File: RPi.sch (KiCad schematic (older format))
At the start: 8 parts, among them U3 LMS6002DR2, U4 ECP5, X3 RaspberryPiConnector

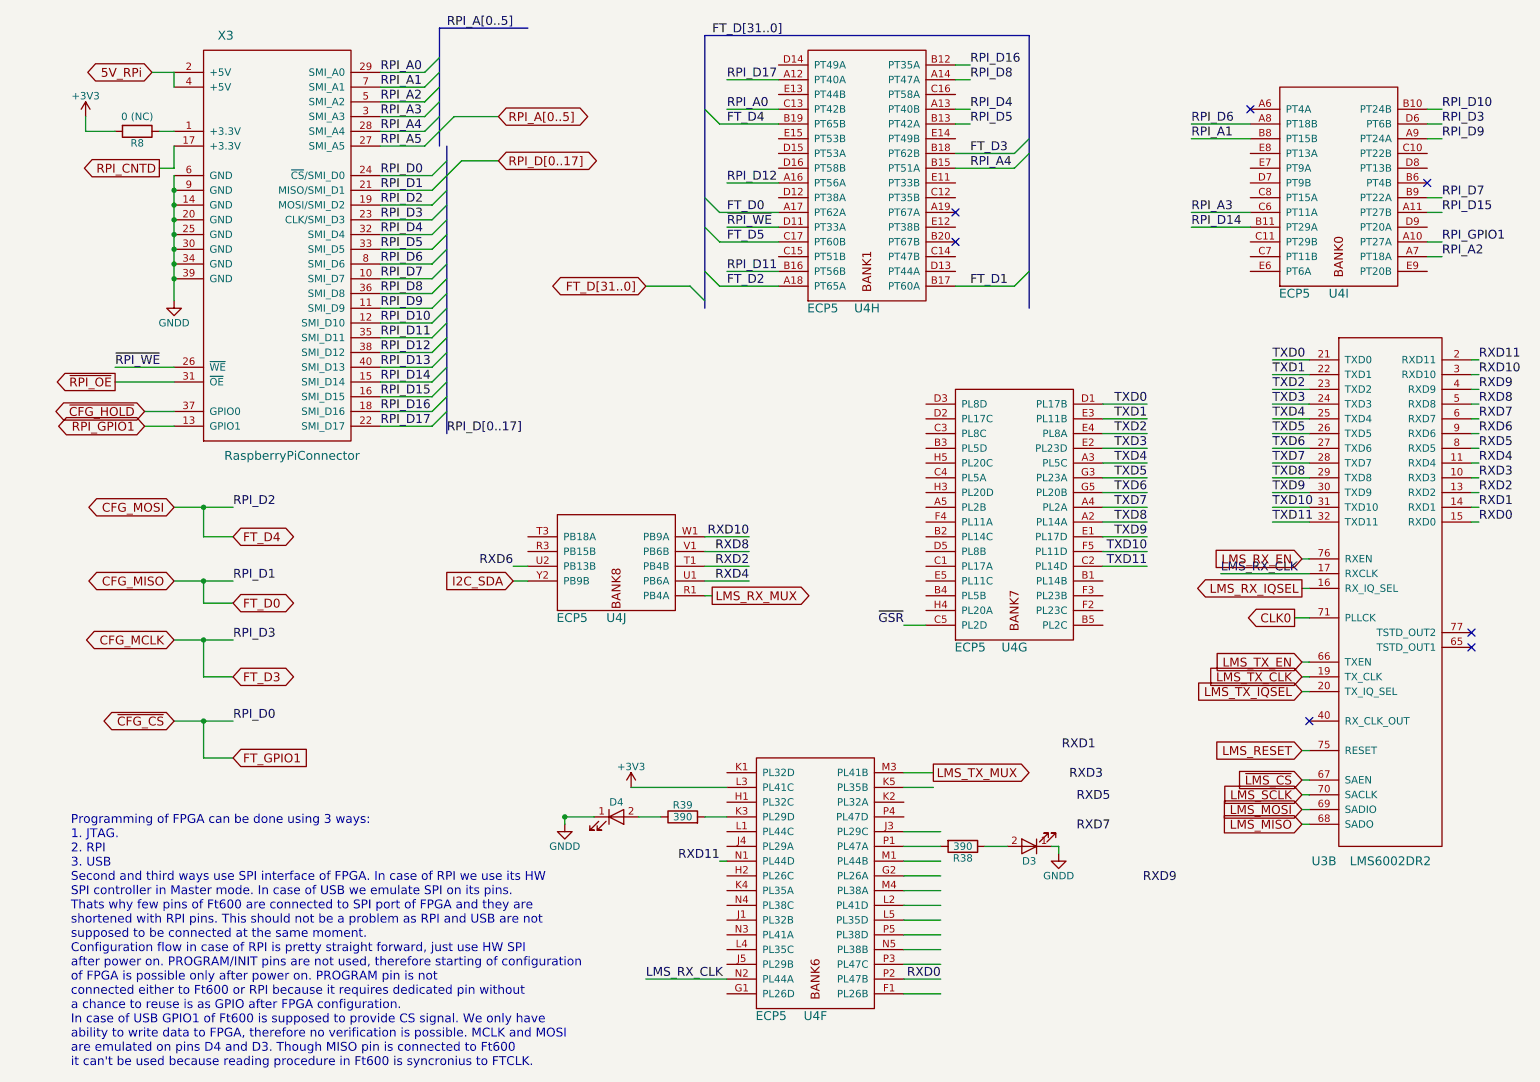
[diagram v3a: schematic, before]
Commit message: Finish tracing IO
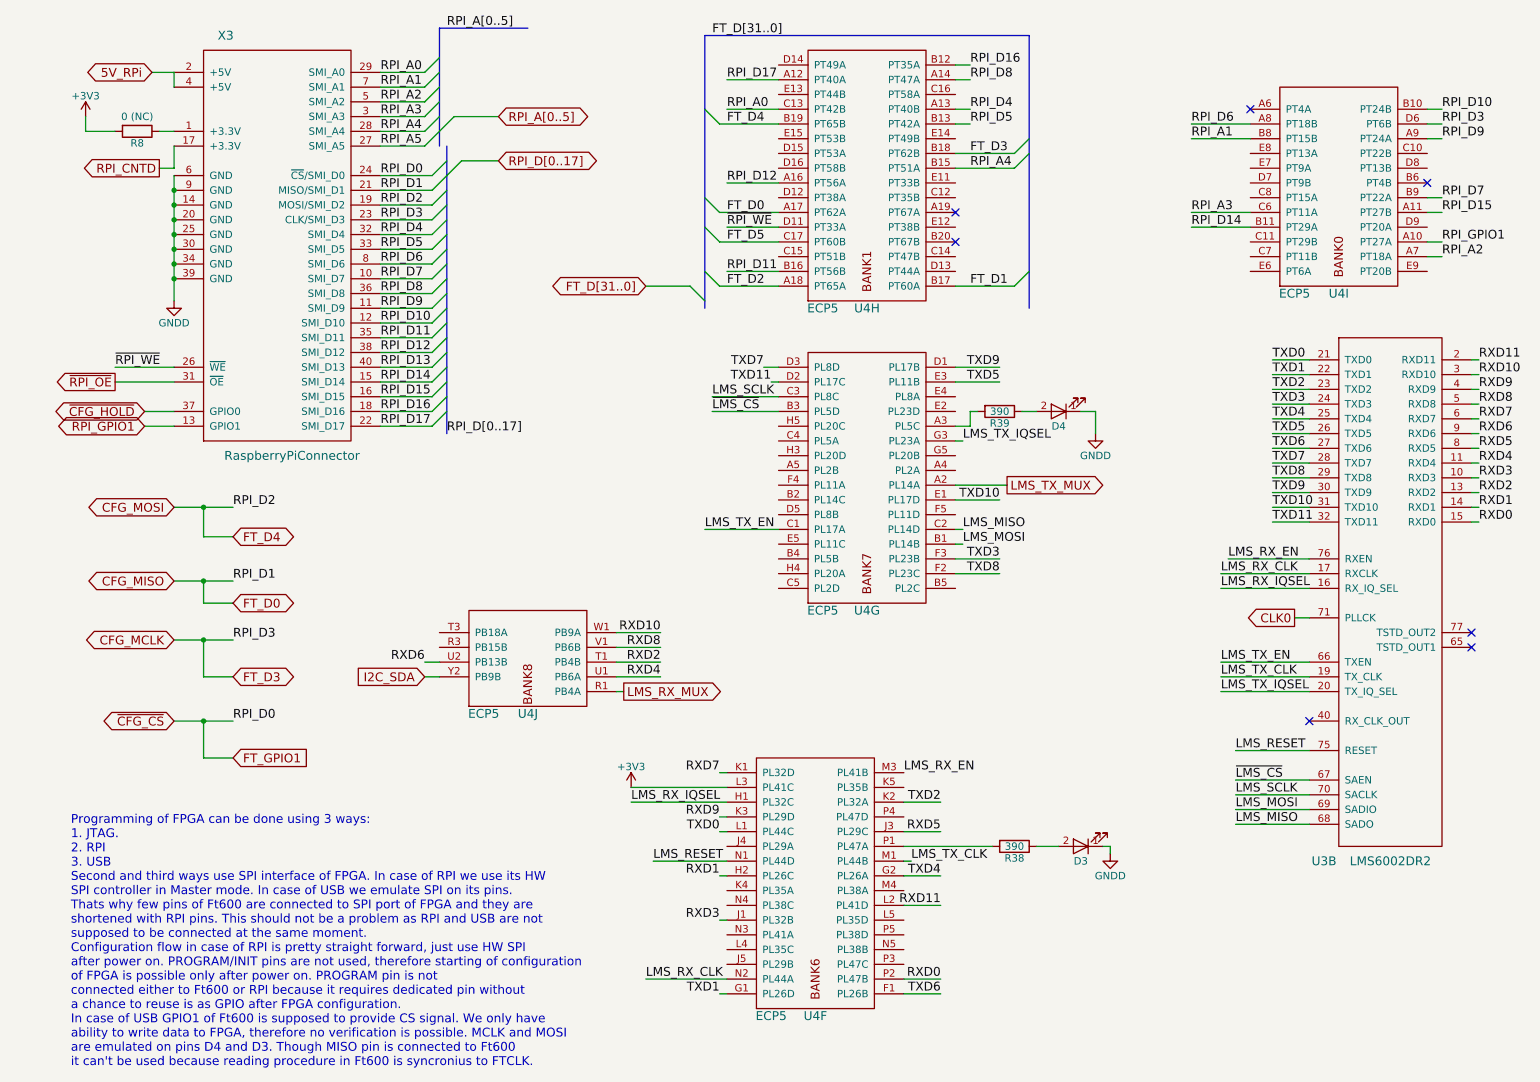
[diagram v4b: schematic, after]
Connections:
- net labels removed: ~GSR
- wire segments 158 -> 163
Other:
- moved on the sheet: D3, D4, R38, R39, U4G, U4J

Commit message: Changed couple of pins
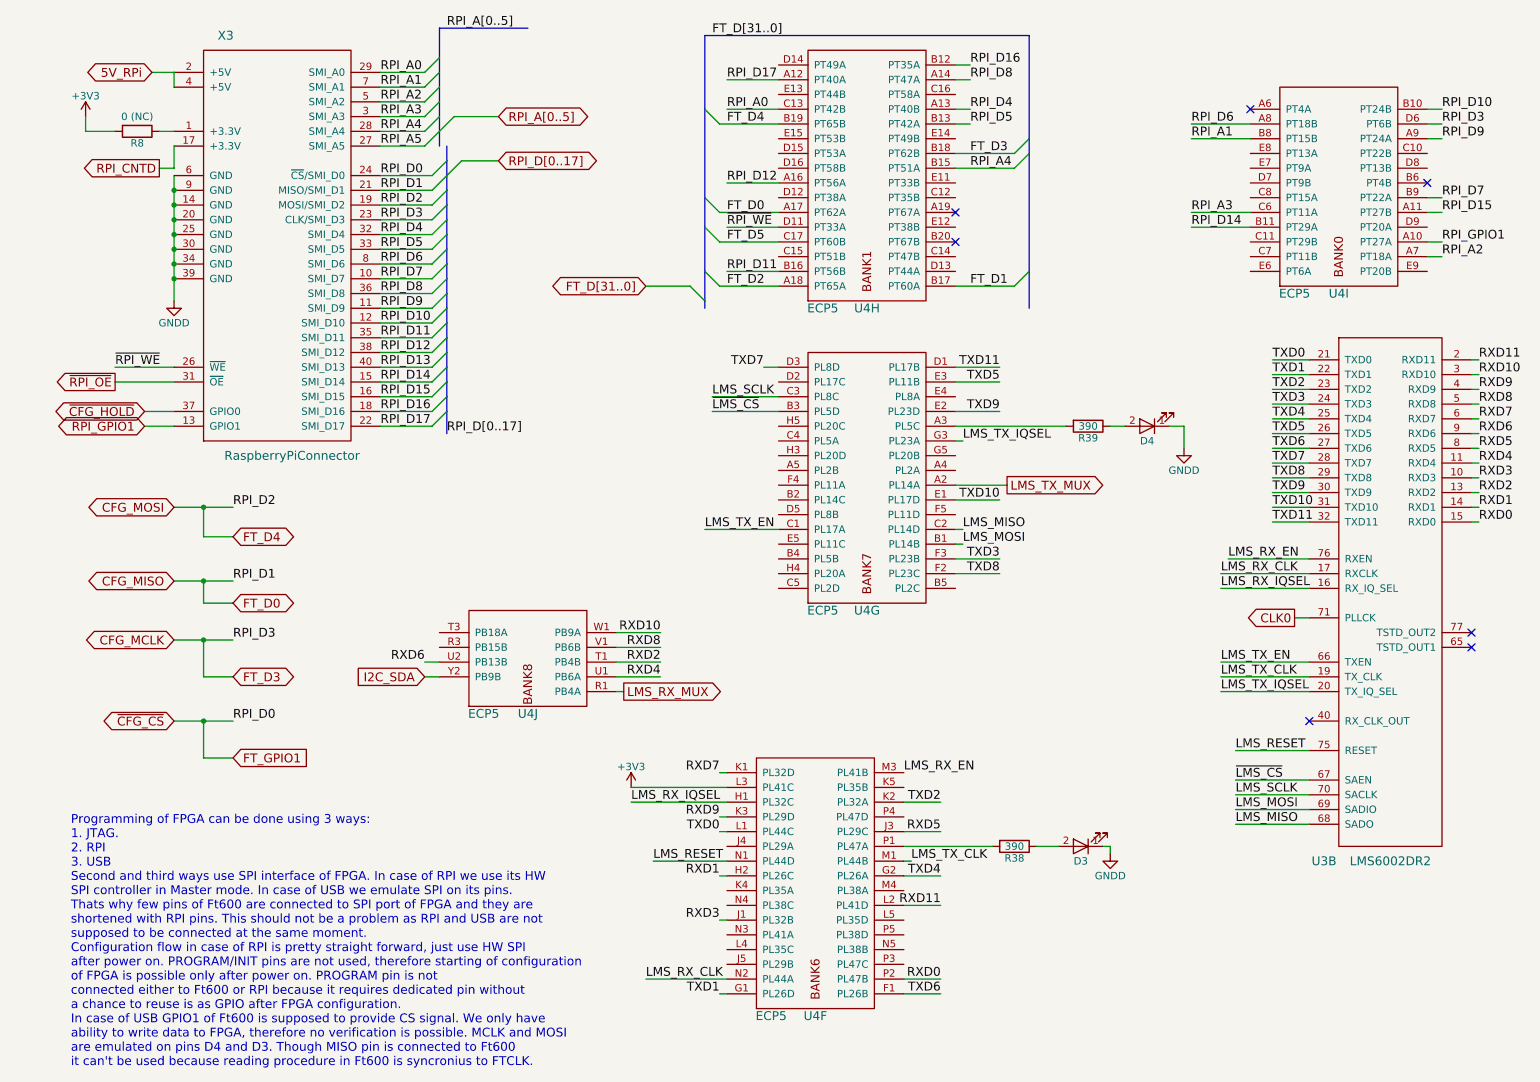
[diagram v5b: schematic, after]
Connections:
- net TXD11: now also U4.D1 (PL17B); no longer U4.D2 (PL17C)
- net TXD9: now also U4.E2 (PL23D); no longer U4.D1 (PL17B)
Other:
- moved on the sheet: D4, R39
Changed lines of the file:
@@
 	1400 950  1400 1050
 Wire Wire Line
-	1400 1650 1400 2500
+	1400 1650 1400 1750
+Wire Wire Line
+	1400 1750 1400 1850
+Wire Wire Line
+	1400 1850 1400 1950
+Wire Wire Line
+	1400 1950 1400 2050
+Wire Wire Line
+	1400 2050 1400 2150
+Wire Wire Line
+	1400 2150 1400 2250
+Wire Wire Line
+	1400 2250 1400 2350
+Wire Wire Line
+	1400 2350 1400 2500
 Connection ~ 1400 1750
 Connection ~ 1400 1850
@@
 	1000 1350 800  1350
 Wire Bus Line
-	3250 1450 3250 3400
+	3250 1450 3250 1550
+Wire Bus Line
+	3250 1550 3250 1650
+Wire Bus Line
+	3250 1650 3250 1750
+Wire Bus Line
+	3250 1750 3250 1850
+Wire Bus Line
+	3250 1850 3250 1950
+Wire Bus Line
+	3250 1950 3250 2050
+Wire Bus Line
+	3250 2050 3250 2150
+Wire Bus Line
+	3250 2150 3250 2250
+Wire Bus Line
+	3250 2250 3250 2350
+Wire Bus Line
+	3250 2350 3250 2450
+Wire Bus Line
+	3250 2450 3250 2550
+Wire Bus Line
+	3250 2550 3250 2650
+Wire Bus Line
+	3250 2650 3250 2750
+Wire Bus Line
+	3250 2750 3250 2850
+Wire Bus Line
+	3250 2850 3250 2950
+Wire Bus Line
+	3250 2950 3250 3050
+Wire Bus Line
+	3250 3050 3250 3150
+Wire Bus Line
+	3250 3150 3250 3250
+Wire Bus Line
+	3250 3250 3250 3400
 Wire Wire Line
 	3350 1550 3600 1550
 Wire Wire Line
-	1400 3900 1800 3900
-Wire Wire Line
-	1400 4400 1800 4400
-Wire Wire Line
-	1400 4800 1800 4800
-Wire Wire Line
-	1400 5350 1800 5350
-Wire Bus Line
-	3200 650  3200 1450
+	1400 3900 1600 3900
+Wire Wire Line
+	1600 3900 1800 3900
+Wire Wire Line
+	1400 4400 1600 4400
+Wire Wire Line
+	1600 4400 1800 4400
+Wire Wire Line
+	1400 4800 1600 4800
+Wire Wire Line
+	1600 4800 1800 4800
+Wire Wire Line
+	1400 5350 1600 5350
+Wire Wire Line
+	1600 5350 1800 5350
+Wire Bus Line
+	3200 650  3200 850
+Wire Bus Line
+	3200 850  3200 950
+Wire Bus Line
+	3200 950  3200 1050
+Wire Bus Line
+	3200 1050 3200 1150
+Wire Bus Line
+	3200 1150 3200 1250
+Wire Bus Line
+	3200 1250 3200 1350
+Wire Bus Line
+	3200 1350 3200 1450
 Wire Bus Line
 	3200 650  3800 650
@@
 	1400 1600 1400 1450
 Wire Bus Line
-	7200 700  7200 2550
-Wire Bus Line
-	5000 700  5000 2550
+	7200 700  7200 1400
+Wire Bus Line
+	7200 1400 7200 1500
+Wire Bus Line
+	7200 1500 7200 2300
+Wire Bus Line
+	7200 2300 7200 2550
+Wire Bus Line
+	5000 700  5000 1200
+Wire Bus Line
+	5000 1200 5000 1800
+Wire Bus Line
+	5000 1800 5000 2000
+Wire Bus Line
+	5000 2000 5000 2300
+Wire Bus Line
+	5000 2300 5000 2500
+Wire Bus Line
+	5000 2500 5000 2550
 $Comp
 L ECP5 U4
@@
 Text Label 7000 4350 2    60   ~ 0
 TXD8
-Text Label 7000 2950 2    60   ~ 0
+Text Label 7000 3250 2    60   ~ 0
 TXD9
 Text Label 7000 3850 2    60   ~ 0
 TXD10
-Text Label 5450 3050 2    60   ~ 0
+Text Label 7000 2950 2    60   ~ 0
 TXD11
 Wire Wire Line
@@
 L LED D4
 U 1 1 5938F77D
-P 7400 3250
-F 0 "D4" H 7400 3350 50  0000 C CNN
-F 1 "5510209F" H 7400 3150 50  0001 C CNN
-F 2 "sdr-foots:LED_IND_SINGLE" H 7400 3250 50  0001 C CNN
-F 3 "" H 7400 3250 50  0001 C CNN
-	1    7400 3250
+P 8000 3350
+F 0 "D4" H 8000 3450 50  0000 C CNN
+F 1 "5510209F" H 8000 3250 50  0001 C CNN
+F 2 "sdr-foots:LED_IND_SINGLE" H 8000 3350 50  0001 C CNN
+F 3 "" H 8000 3350 50  0001 C CNN
+	1    8000 3350
 	-1   0    0    1
 $EndComp
@@
 L R R39
 U 1 1 5938F9FB
-P 7000 3250
-F 0 "R39" V 7080 3250 50  0000 C CNN
-F 1 "390" V 7000 3250 50  0000 C CNN
-F 2 "Resistors_SMD:R_0603" V 6930 3250 50  0001 C CNN
-F 3 "" H 7000 3250 50  0001 C CNN
-	1    7000 3250
+P 7600 3350
+F 0 "R39" V 7680 3350 50  0000 C CNN
+F 1 "390" V 7600 3350 50  0000 C CNN
+F 2 "Resistors_SMD:R_0603" V 7530 3350 50  0001 C CNN
+F 3 "" H 7600 3350 50  0001 C CNN
+	1    7600 3350
 	0    1    1    0
 $EndComp
@@
 L GNDD #PWR041
 U 1 1 5938FEB2
-P 7650 3400
-F 0 "#PWR041" H 7650 3150 50  0001 C CNN
-F 1 "GNDD" H 7650 3250 50  0000 C CNN
-F 2 "" H 7650 3400 50  0001 C CNN
-F 3 "" H 7650 3400 50  0001 C CNN
-	1    7650 3400
+P 8250 3500
+F 0 "#PWR041" H 8250 3250 50  0001 C CNN
+F 1 "GNDD" H 8250 3350 50  0000 C CNN
+F 2 "" H 8250 3500 50  0001 C CNN
+F 3 "" H 8250 3500 50  0001 C CNN
+	1    8250 3500
 	1    0    0    -1
 $EndComp
@@
 Wire Wire Line
 	5500 2950 5400 2950
-Wire Wire Line
-	5500 3050 5450 3050
 Text Label 8500 4950 0    60   ~ 0
 LMS_TX_EN
@@
 	5050 3250 5500 3250
 Wire Wire Line
-	7650 3400 7650 3250
-Wire Wire Line
-	7650 3250 7550 3250
-Wire Wire Line
-	7250 3250 7150 3250
+	8250 3500 8250 3350
+Wire Wire Line
+	8250 3350 8150 3350
+Wire Wire Line
+	7850 3350 7750 3350
 Wire Wire Line
 	6750 4150 6700 4150
@@
 LMS_MOSI
 Wire Wire Line
-	6700 3350 6800 3350
-Wire Wire Line
-	6800 3350 6800 3250
-Wire Wire Line
-	6800 3250 6850 3250
-Wire Wire Line
 	7050 3750 6700 3750
+Wire Wire Line
+	7450 3350 6700 3350
+Wire Wire Line
+	7000 3250 6700 3250
 $EndSCHEMATC

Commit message: FT232H has been finished Not finished: - PROGRAMN button - silkscreen preparation - RF
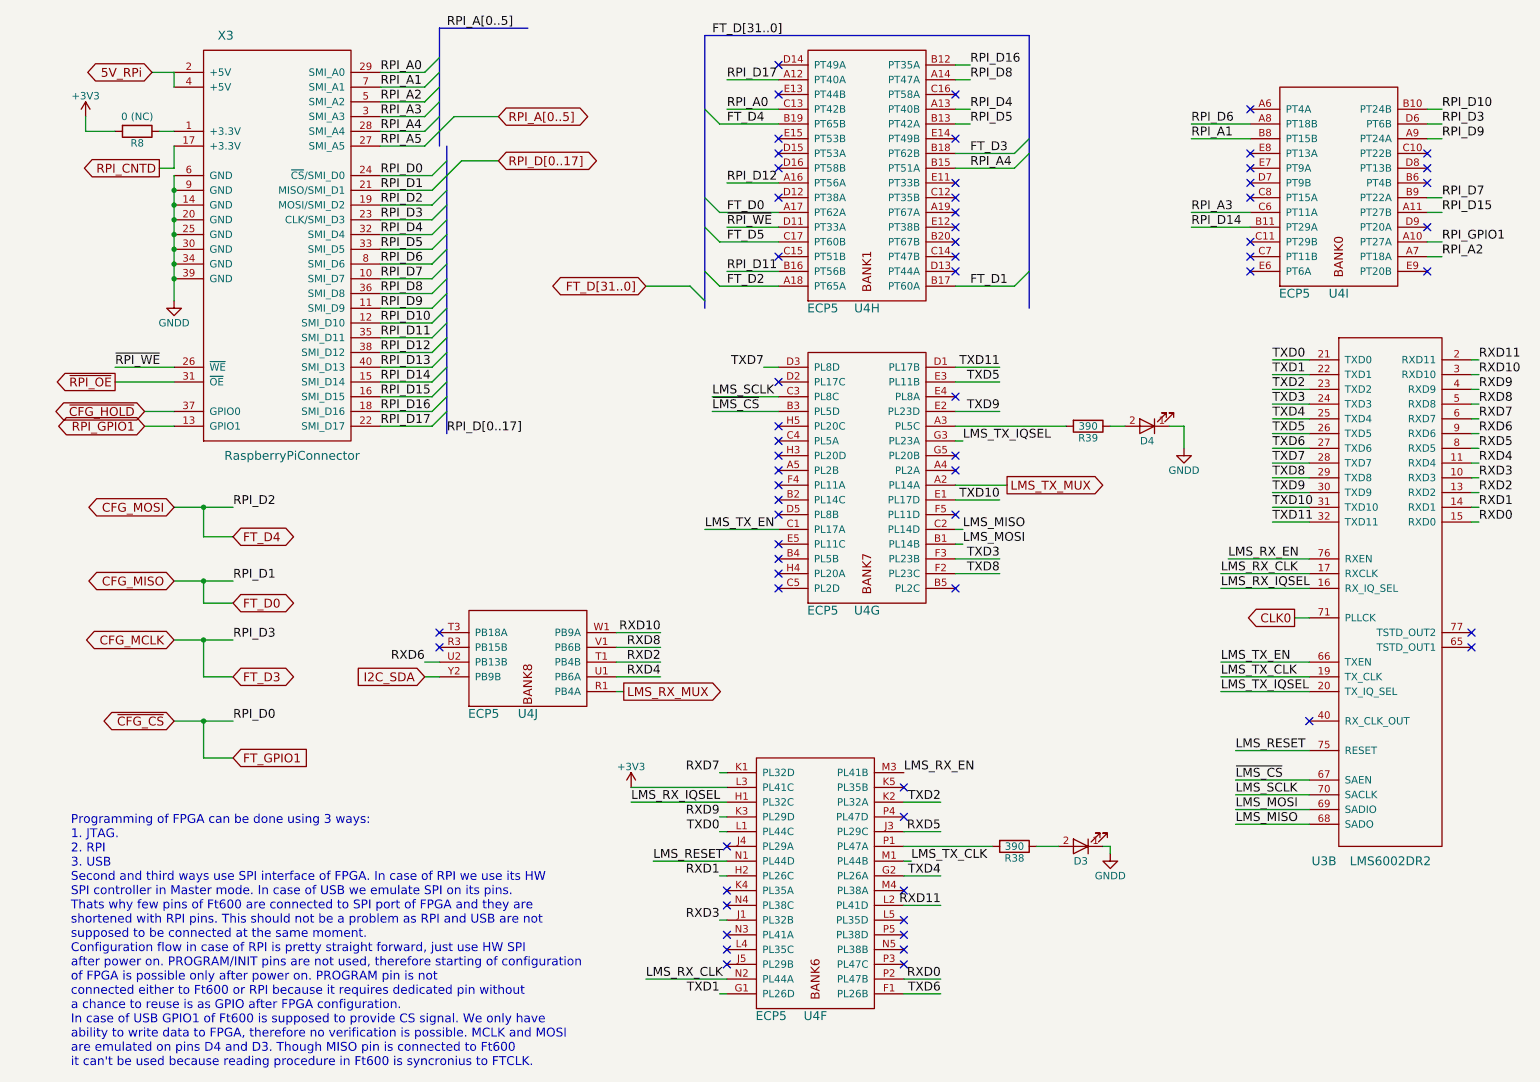
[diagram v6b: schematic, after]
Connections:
- no-connect marks 7 -> 64
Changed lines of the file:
@@
 	1400 950  1400 1050
 Wire Wire Line
-	1400 1650 1400 1750
-Wire Wire Line
-	1400 1750 1400 1850
-Wire Wire Line
-	1400 1850 1400 1950
-Wire Wire Line
-	1400 1950 1400 2050
-Wire Wire Line
-	1400 2050 1400 2150
-Wire Wire Line
-	1400 2150 1400 2250
-Wire Wire Line
-	1400 2250 1400 2350
-Wire Wire Line
-	1400 2350 1400 2500
+	1400 1650 1400 2500
 Connection ~ 1400 1750
 Connection ~ 1400 1850
@@
 	1000 1350 800  1350
 Wire Bus Line
-	3250 1450 3250 1550
+	3250 1450 3250 3400
+Wire Wire Line
+	3350 1550 3600 1550
+Wire Wire Line
+	1400 3900 1800 3900
+Wire Wire Line
+	1400 4400 1800 4400
+Wire Wire Line
+	1400 4800 1800 4800
+Wire Wire Line
+	1400 5350 1800 5350
 Wire Bus Line
-	3250 1550 3250 1650
-Wire Bus Line
-	3250 1650 3250 1750
-Wire Bus Line
-	3250 1750 3250 1850
-Wire Bus Line
-	3250 1850 3250 1950
-Wire Bus Line
-	3250 1950 3250 2050
-Wire Bus Line
-	3250 2050 3250 2150
-Wire Bus Line
-	3250 2150 3250 2250
-Wire Bus Line
-	3250 2250 3250 2350
-Wire Bus Line
-	3250 2350 3250 2450
-Wire Bus Line
-	3250 2450 3250 2550
-Wire Bus Line
-	3250 2550 3250 2650
-Wire Bus Line
-	3250 2650 3250 2750
-Wire Bus Line
-	3250 2750 3250 2850
-Wire Bus Line
-	3250 2850 3250 2950
-Wire Bus Line
-	3250 2950 3250 3050
-Wire Bus Line
-	3250 3050 3250 3150
-Wire Bus Line
-	3250 3150 3250 3250
-Wire Bus Line
-	3250 3250 3250 3400
-Wire Wire Line
-	3350 1550 3600 1550
-Wire Wire Line
-	1400 3900 1600 3900
-Wire Wire Line
-	1600 3900 1800 3900
-Wire Wire Line
-	1400 4400 1600 4400
-Wire Wire Line
-	1600 4400 1800 4400
-Wire Wire Line
-	1400 4800 1600 4800
-Wire Wire Line
-	1600 4800 1800 4800
-Wire Wire Line
-	1400 5350 1600 5350
-Wire Wire Line
-	1600 5350 1800 5350
-Wire Bus Line
-	3200 650  3200 850
-Wire Bus Line
-	3200 850  3200 950
-Wire Bus Line
-	3200 950  3200 1050
-Wire Bus Line
-	3200 1050 3200 1150
-Wire Bus Line
-	3200 1150 3200 1250
-Wire Bus Line
-	3200 1250 3200 1350
-Wire Bus Line
-	3200 1350 3200 1450
+	3200 650  3200 1450
 Wire Bus Line
 	3200 650  3800 650
@@
 	1400 1600 1400 1450
 Wire Bus Line
-	7200 700  7200 1400
+	7200 700  7200 2550
 Wire Bus Line
-	7200 1400 7200 1500
-Wire Bus Line
-	7200 1500 7200 2300
-Wire Bus Line
-	7200 2300 7200 2550
-Wire Bus Line
-	5000 700  5000 1200
-Wire Bus Line
-	5000 1200 5000 1800
-Wire Bus Line
-	5000 1800 5000 2000
-Wire Bus Line
-	5000 2000 5000 2300
-Wire Bus Line
-	5000 2300 5000 2500
-Wire Bus Line
-	5000 2500 5000 2550
+	5000 700  5000 2550
 $Comp
 L ECP5 U4
@@
 Wire Wire Line
 	7000 3250 6700 3250
+NoConn ~ 3200 4750
+NoConn ~ 3200 4850
+NoConn ~ 6350 5800
+NoConn ~ 6350 6000
+NoConn ~ 6350 6500
+NoConn ~ 6350 6700
+NoConn ~ 6350 6800
+NoConn ~ 6350 6900
+NoConn ~ 6350 7000
+NoConn ~ 5150 7000
+NoConn ~ 5150 6900
+NoConn ~ 5150 6800
+NoConn ~ 5150 6600
+NoConn ~ 5150 6500
+NoConn ~ 5150 6200
+NoConn ~ 5500 3350
+NoConn ~ 5500 3450
+NoConn ~ 5500 3550
+NoConn ~ 5500 3650
+NoConn ~ 5500 3750
+NoConn ~ 5500 3850
+NoConn ~ 5500 3950
+NoConn ~ 5500 4150
+NoConn ~ 5500 4250
+NoConn ~ 5500 4350
+NoConn ~ 5500 4450
+NoConn ~ 6700 4450
+NoConn ~ 6700 3550
+NoConn ~ 6700 3650
+NoConn ~ 6700 3950
+NoConn ~ 6700 3150
+NoConn ~ 5500 3050
+NoConn ~ 9900 1500
+NoConn ~ 9900 1600
+NoConn ~ 9900 2000
+NoConn ~ 9900 2300
+NoConn ~ 8700 1500
+NoConn ~ 8700 1600
+NoConn ~ 8700 1700
+NoConn ~ 8700 1800
+NoConn ~ 8700 2100
+NoConn ~ 8700 2200
+NoConn ~ 8700 2300
+NoConn ~ 5500 900
+NoConn ~ 5500 1100
+NoConn ~ 5500 1400
+NoConn ~ 5500 1500
+NoConn ~ 5500 1600
+NoConn ~ 5500 1800
+NoConn ~ 5500 2200
+NoConn ~ 6700 1100
+NoConn ~ 6700 1400
+NoConn ~ 6700 1700
+NoConn ~ 6700 1800
+NoConn ~ 6700 2000
+NoConn ~ 6700 2200
+NoConn ~ 6700 2300
 $EndSCHEMATC
